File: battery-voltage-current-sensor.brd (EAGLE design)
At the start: 100 x 100 mm, 46 parts, among them IC1 ACS758LCB-050B-PFF-T, IC3 ADS1115IDGST

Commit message: first placing succes
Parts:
- added D1: C78395, diode:SMB
- added D3, D4, D5, D6: KT-0603R, SMD-LED-CLEAR-BLUE_0603_:LED-0603
- added R10, R12: C13564, rcl:R0603
- added R11, R9: 10k, rcl:R0603
- added R14, R25, R26, R27: 1k, rcl:R0805
- moved R6 9.98 mm to (83.9, 93.4), turned to 0 degrees
- moved C2 9.90 mm to (88.1, 4.80), turned to 90 degrees
- moved R5 8.51 mm to (83.9, 95.5), turned to 0 degrees
- moved C4 7.69 mm to (76.5, 92.3), turned to 180 degrees
- moved C11 7.32 mm to (80.8, 92.9), turned to 270 degrees
- moved C10 4.72 mm to (80.8, 96.0)
- moved IC3 4.46 mm to (76.6, 95.2), turned to 0 degrees
- moved R8 3.34 mm to (69.3, 95.4), turned to 180 degrees
- moved R7 2.86 mm to (69.3, 93.3), turned to 180 degrees
- moved C12 2.84 mm to (72.4, 92.8), turned to 270 degrees
- moved C13 2.62 mm to (72.4, 95.9)
- moved C1 2.40 mm to (70.1, 5.00)
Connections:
- removed net SIGNALHV: R24.2, R4.1
- new net N$17: D6.+, R27.1
- new net N$19: R14.2, U$1.JP1.6
- new net N$20: R25.2, U$1.JP1.5
- new net N$21: R26.2, U$1.JP1.4
- new net N$6: D4.+, R25.1
- new net VOUTHV: R24.2, R4.1, R8.2
- new net VOUTNTC1: R10.2, R6.2, R9.1
- new net VOUTNTC2: R11.1, R12.2, R5.2
- net +5V/1: now also D1.C, R11.2, R9.2
- net GND: now also D1.A, D3.-, D4.-, D5.-, D6.-, R10.1, R12.1
- net HV-: no longer R24.1
- net HV-IN: now also R24.1
- net N$18: now also R27.2, U$1.JP1.7; no longer R7.2
- net N$3: now also D3.+, R14.1; no longer R5.2
- net N$7: now also D5.+, R26.1; no longer R6.2
- net VOUTCURRENT: now also R7.2; no longer R8.2
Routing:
- net +5V/1: track 0.00 -> 148.7 mm, vias 0 -> 1
- net +12V/1: track 0.00 -> 93.6 mm
- net N$1: track 0.00 -> 89.7 mm, vias 0 -> 2
- net N$5: track 0.00 -> 87.9 mm, vias 0 -> 2
- net N$4: track 0.00 -> 85.5 mm, vias 0 -> 2
- net VOUTNTC1: track 0.00 -> 69.0 mm, vias 0 -> 2
- net VOUTHV: track 0.00 -> 58.1 mm
- net GND: track 0.00 -> 42.6 mm
- net +3.3V/1: track 0.00 -> 26.9 mm, vias 0 -> 1
- net N$7: track 0.00 -> 25.6 mm
- net N$6: track 0.00 -> 22.2 mm
- net N$3: track 0.00 -> 19.9 mm
- net N$17: track 0.00 -> 17.5 mm
- net VOUTCURRENT: track 0.00 -> 16.2 mm
- net HV-IN: track 0.00 -> 14.2 mm
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- added copper zone on layer 1, net GND
- added copper zone on layer 16, net GND

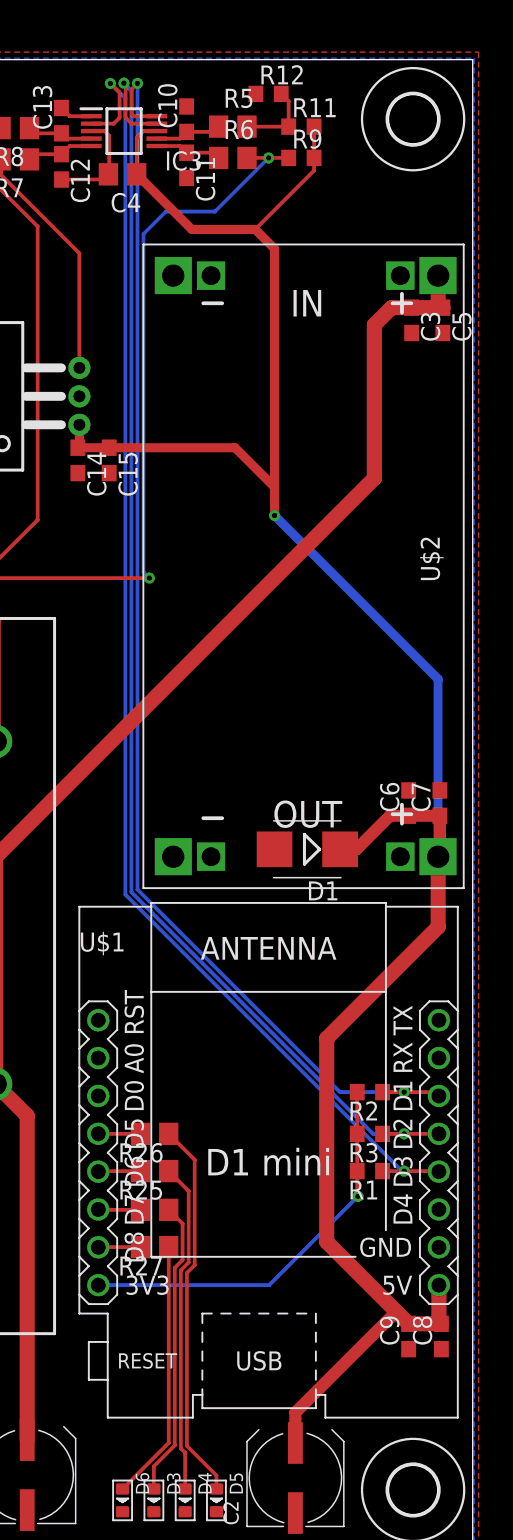
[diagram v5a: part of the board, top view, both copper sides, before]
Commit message: level shifter added
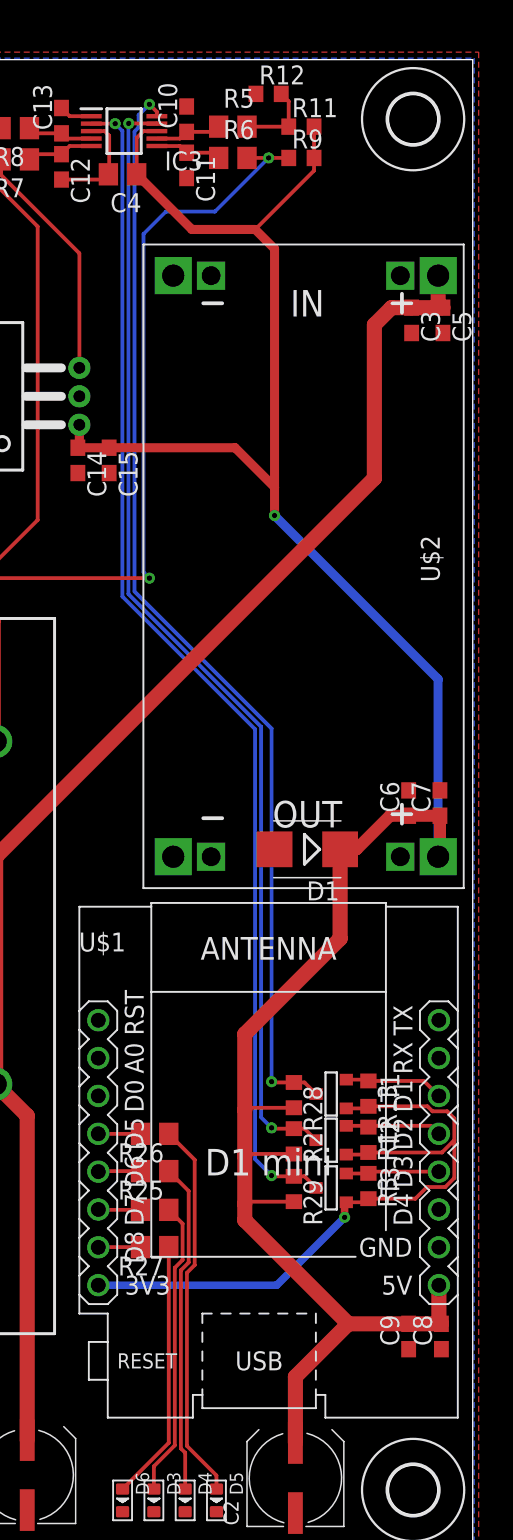
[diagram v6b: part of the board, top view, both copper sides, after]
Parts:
- added R13, R28, R29: 10k, rcl:R0603
- added T1, T2, T3: C8545, zetex:SOT-23
- moved R2 6.07 mm to (88.0, 27.4), turned to 270 degrees
- moved R3 3.50 mm to (93.0, 24.4), turned to 270 degrees
- moved R1 2.10 mm to (93.0, 27.5), turned to 270 degrees
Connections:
- removed net N$4: IC3.10, R2.1, U$1.JP2.3
- new net ALERT: IC3.2, R29.1, T3.1
- new net N$2: R13.1, T1.2, U$1.JP2.3
- new net SCL: IC3.10, R28.1, T1.1
- new net SDA: IC3.9, R2.1, T2.1
- net +3.3V/1: now also R13.2, T1.3, T2.3, T3.3; no longer R2.2
- net +5V/1: now also R2.2, R28.2, R29.2
- net N$1: now also T2.2, U$1.JP2.4; no longer IC3.2, U$1.JP2.5
- net N$5: now also T3.2, U$1.JP2.5; no longer IC3.9, U$1.JP2.4
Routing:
- net N$4: track 85.5 -> 0.00 mm, vias 2 -> 0
- net N$1: track 89.7 -> 6.56 mm, vias 2 -> 0
- net N$5: track 87.9 -> 6.27 mm, vias 2 -> 0
- net ALERT: track 0.00 -> 79.9 mm, vias 0 -> 2
- net SDA: track 0.00 -> 76.6 mm, vias 0 -> 2
- net SCL: track 0.00 -> 74.2 mm, vias 0 -> 2
- net +3.3V/1: track 26.9 -> 46.7 mm
- net +5V/1: track 148.7 -> 161.4 mm
- net N$2: track 0.00 -> 6.67 mm

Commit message: first draft of production data generated
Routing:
- net HV-: track 115.2 -> 73.3 mm
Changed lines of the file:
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@@
 <contactref element="IC1" pad="IP-@9" route="any" routetag="G$1.IP-"/>
 <contactref element="PS1" pad="1"/>
-<wire x1="50" y1="6" x2="50" y2="42.74" width="5" layer="16"/>
-<wire x1="50" y1="40.24" x2="50" y2="68.2" width="5" layer="16"/>
-<wire x1="50" y1="68.2" x2="52.2" y2="70.4" width="5" layer="16"/>
-<wire x1="5.89" y1="42.74" x2="50" y2="42.74" width="1" layer="16"/>
 <polygon width="0" layer="16" thermals="no">
 <vertex x="56" y="77"/>
@@
 <vertex x="56" y="0"/>
 </polygon>
-<wire x1="49.878" y1="72.722" x2="52.2" y2="70.4" width="0.3048" layer="1"/>
+<wire x1="5.89" y1="42.74" x2="37.06" y2="42.74" width="1.016" layer="16"/>
+<wire x1="50" y1="29.8" x2="50" y2="6" width="1.016" layer="16"/>
+<wire x1="37.06" y1="42.74" x2="50" y2="29.8" width="1.016" layer="16"/>
 </signal>
 <signal name="N$8">

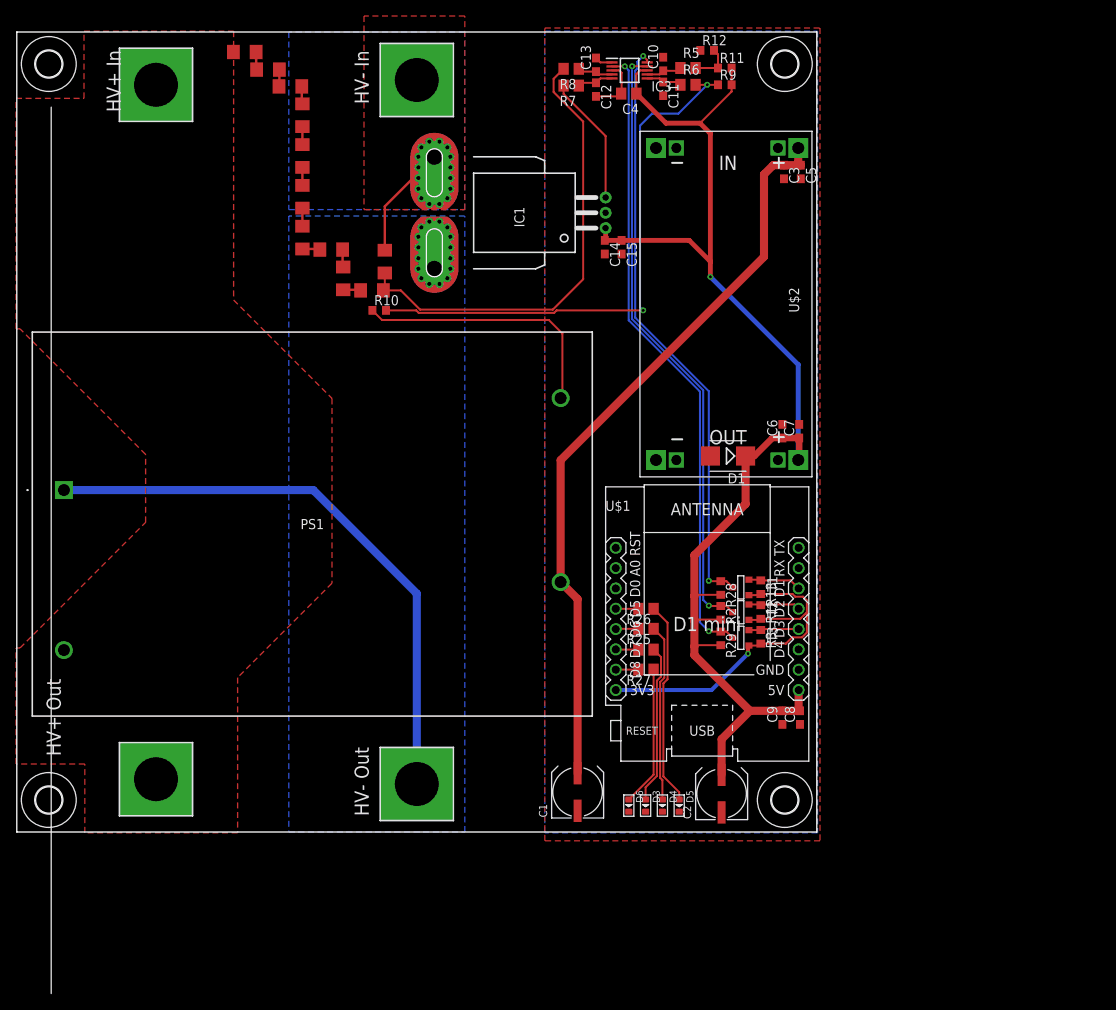
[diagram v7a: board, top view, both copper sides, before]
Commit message: external 12V added
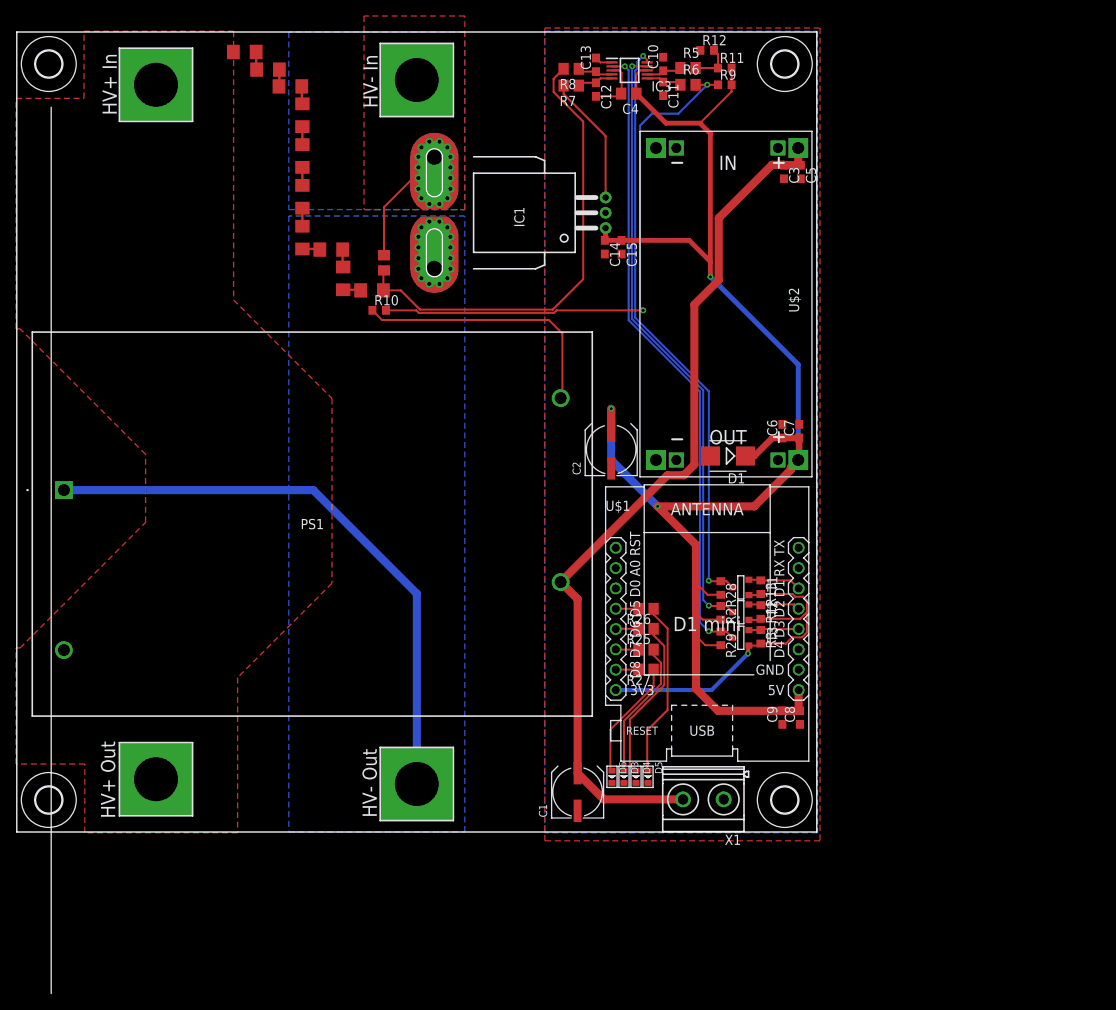
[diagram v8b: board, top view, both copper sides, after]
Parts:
- added X1: MKDSN1,5/2-5,08, con-phoenix-508:MKDSN1,5/2-5,08
- C2: value (none) -> C473426
- R15, R16, R17, R18, R19, R20, R21, R22, R23, R4: value 120k -> C17902
- R24: value 10k 1206 -> C17772; device rcl:R1206 -> rcl:R0805
- moved C2 45.2 mm to (74.3, 47.8)
- moved D5 5.31 mm to (78.9, 6.90)
- moved D4 4.88 mm to (77.4, 6.90)
- moved D3 4.50 mm to (75.9, 6.90)
- moved D6 4.17 mm to (74.4, 6.90)
- moved R24 0.18 mm to (45.9, 71.2)
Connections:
- net +12V/1: now also X1.2
- net GND: now also X1.1
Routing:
- net +5V/1: track 161.4 -> 185.3 mm, vias 1 -> 3
- net +12V/1: track 93.6 -> 109.5 mm
- net N$7: track 25.6 -> 22.1 mm
- net N$17: track 17.5 -> 15.0 mm
- net N$3: track 19.9 -> 17.4 mm
- net N$6: track 22.2 -> 20.4 mm
- net HV-IN: track 14.2 -> 14.9 mm
